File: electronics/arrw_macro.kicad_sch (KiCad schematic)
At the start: 15 parts, among them J13 Conn_01x04, J14 Conn_01x04, J15 Conn_01x04, J16 Conn_01x04, SW59 SW_SPST, SW60 SW_SPST, SW61 SW_SPST, SW62 SW_SPST, SW63 SW_SPST, SW64 SW_SPST, SW65 SW_SPST, SW66 SW_SPST, SW67 SW_SPST, SW68 SW_SPST, U4 MAX7314AEG+

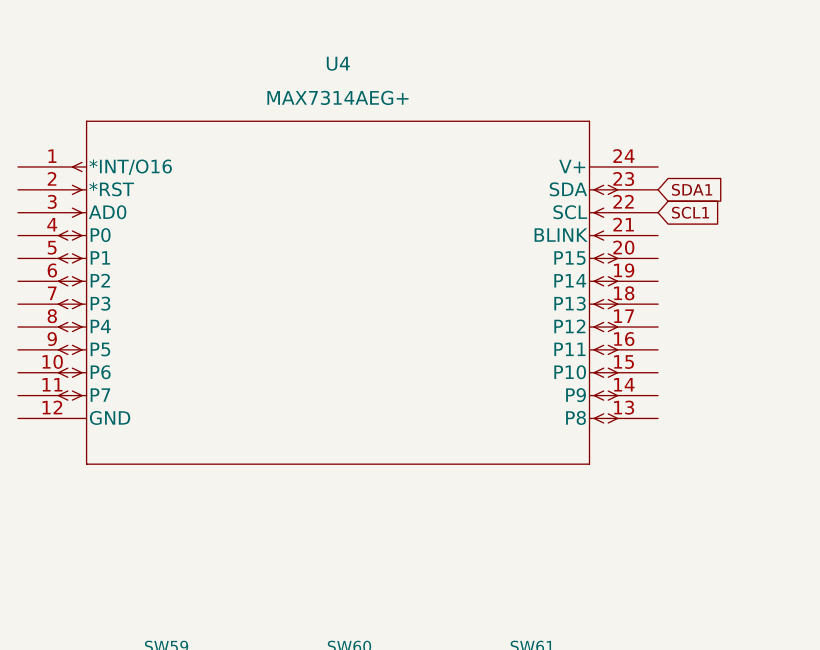
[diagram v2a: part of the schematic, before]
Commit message: change IO expander
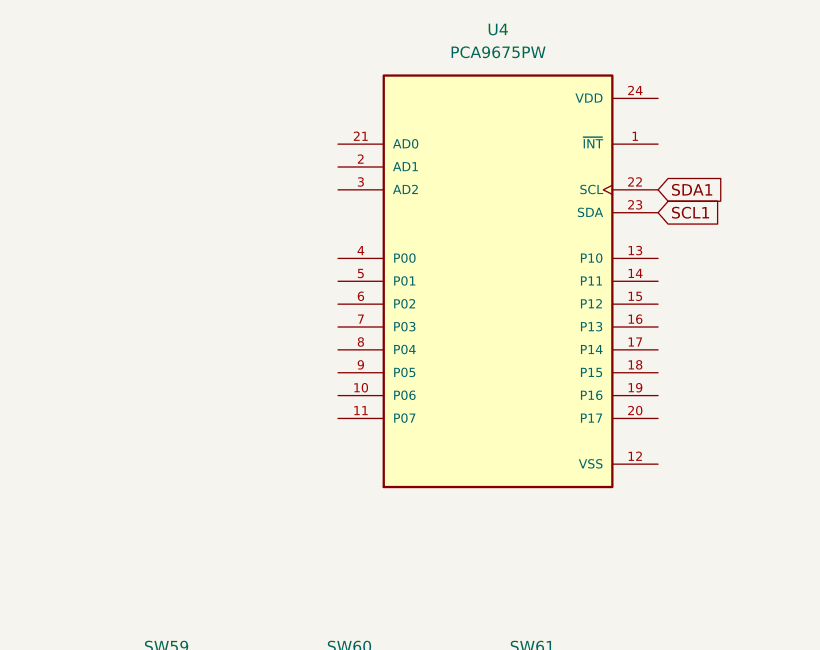
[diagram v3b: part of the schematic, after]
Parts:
- removed U4: MAX7314AEG+, MAX7314AEG:MAX7314AEG&plus_, symbol MAX7314AEG:MAX7314AEG+
- added U4: PCA9675PW, PCA9675PW:SOP65P640X110-24N, symbol PCA9675PW_118:PCA9675PW
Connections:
- net SCL1: now also U4.23 (SDA)
- net SDA1: now also U4.22 (SCL)
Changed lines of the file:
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@@
     (pin "1")
   )
-  (symbol (lib_id "MAX7314AEG:MAX7314AEG+") (at 52.07 46.99 0) (unit 1)
+  (symbol (lib_id "power:GND") (at 205.74 78.74 270) (unit 1)
     (in_bom yes) (on_board yes) (fields_autoplaced)
-    (property "Reference" "U4" (id 0) (at 87.63 35.56 0)
-      (effects (font (size 1.524 1.524)))
+    (property "Reference" "#PWR035" (id 0) (at 199.39 78.74 0)
+      (effects (font (size 1.27 1.27)) hide)
     )
-    (property "Value" "MAX7314AEG+" (id 1) (at 87.63 39.37 0)
-      (effects (font (size 1.524 1.524)))
+    (property "Value" "GND" (id 1) (at 201.93 78.7399 90)
+      (effects (font (size 1.27 1.27)) (justify right))
     )
-    (property "Footprint" "MAX7314AEG:MAX7314AEG&plus_" (id 2) (at 87.63 40.894 0)
-      (effects (font (size 1.524 1.524)) hide)
+    (property "Footprint" "" (id 2) (at 205.74 78.74 0)
+      (effects (font (size 1.27 1.27)) hide)
     )
-    (property "Datasheet" "${OSHMOUNT_LIBRARY}/MAX7314AEG/MAX7314AEG+.pdf" (id 3) (at 52.07 46.99 0)
-      (effects (font (size 1.524 1.524)) hide)
+    (property "Datasheet" "" (id 3) (at 205.74 78.74 0)
+      (effects (font (size 1.27 1.27)) hide)
+    )
+    (pin "1")
+  )
+  (symbol (lib_id "PCA9675PW_118:PCA9675PW") (at 105.41 59.69 0) (unit 1)
+    (in_bom yes) (on_board yes) (fields_autoplaced)
+    (property "Reference" "U4" (id 0) (at 105.41 31.75 0))
+    (property "Value" "PCA9675PW" (id 1) (at 105.41 34.29 0))
+    (property "Footprint" "PCA9675PW:SOP65P640X110-24N" (id 2) (at 105.41 59.69 0)
+      (effects (font (size 1.27 1.27)) (justify left bottom) hide)
+    )
+    (property "Datasheet" "${OSHMOUNT_LIBRARY}/PCA9675PW/datasheet.pdf" (id 3) (at 105.41 59.69 0)
+      (effects (font (size 1.27 1.27)) (justify left bottom) hide)
+    )
+    (property "E1_NOM" "4.4" (id 4) (at 105.41 59.69 0)
+      (effects (font (size 1.27 1.27)) (justify left bottom) hide)
+    )
+    (property "L1_MIN" "" (id 5) (at 105.41 59.69 0)
+      (effects (font (size 1.27 1.27)) (justify left bottom) hide)
+    )
+    (property "D1_NOM" "" (id 6) (at 105.41 59.69 0)
+      (effects (font (size 1.27 1.27)) (justify left bottom) hide)
+    )
+    (property "STANDARD" "IPC 7351B" (id 7) (at 105.41 59.69 0)
+      (effects (font (size 1.27 1.27)) (justify left bottom) hide)
+    )
+    (property "L1_MAX" "" (id 8) (at 105.41 59.69 0)
+      (effects (font (size 1.27 1.27)) (justify left bottom) hide)
+    )
+    (property "PACKAGE_TYPE" "" (id 9) (at 105.41 59.69 0)
+      (effects (font (size 1.27 1.27)) (justify left bottom) hide)
+    )
+    (property "PINS" "" (id 10) (at 105.41 59.69 0)
+      (effects (font (size 1.27 1.27)) (justify left bottom) hide)
+    )
+    (property "B_NOM" "0.245" (id 11) (at 105.41 59.69 0)
+      (effects (font (size 1.27 1.27)) (justify left bottom) hide)
+    )
+    (property "A1_MIN" "0.05" (id 12) (at 105.41 59.69 0)
+      (effects (font (size 1.27 1.27)) (justify left bottom) hide)
+    )
+    (property "D_MAX" "7.9" (id 13) (at 105.41 59.69 0)
+      (effects (font (size 1.27 1.27)) (justify left bottom) hide)
+    )
+    (property "D_MIN" "7.7" (id 14) (at 105.41 59.69 0)
+      (effects (font (size 1.27 1.27)) (justify left bottom) hide)
+    )
+    (property "E_MIN" "6.2" (id 15) (at 105.41 59.69 0)
+      (effects (font (size 1.27 1.27)) (justify left bottom) hide)
+    )
+    (property "VACANCIES" "" (id 16) (at 105.41 59.69 0)
+      (effects (font (size 1.27 1.27)) (justify left bottom) hide)
+    )
+    (property "E1_MIN" "4.3" (id 17) (at 105.41 59.69 0)
+      (effects (font (size 1.27 1.27)) (justify left bottom) hide)
+    )
+    (property "SNAPEDA_PACKAGE_ID" "" (id 18) (at 105.41 59.69 0)
+      (effects (font (size 1.27 1.27)) (justify left bottom) hide)
+    )
+    (property "MANUFACTURER" "NXP" (id 19) (at 105.41 59.69 0)
+      (effects (font (size 1.27 1.27)) (justify left bottom) hide)
+    )
+    (property "E1_MAX" "4.5" (id 20) (at 105.41 59.69 0)
+      (effects (font (size 1.27 1.27)) (justify left bottom) hide)
+    )
+    (property "DMIN" "" (id 21) (at 105.41 59.69 0)
+      (effects (font (size 1.27 1.27)) (justify left bottom) hide)
+    )
+    (property "B_MAX" "0.3" (id 22) (at 105.41 59.69 0)
+      (effects (font (size 1.27 1.27)) (justify left bottom) hide)
+    )
+    (property "A_NOM" "1.1" (id 23) (at 105.41 59.69 0)
+      (effects (font (size 1.27 1.27)) (justify left bottom) hide)
+    )
+    (property "D1_MAX" "" (id 24) (at 105.41 59.69 0)
+      (effects (font (size 1.27 1.27)) (justify left bottom) hide)
+    )
+    (property "DNOM" "" (id 25) (at 105.41 59.69 0)
+      (effects (font (size 1.27 1.27)) (justify left bottom) hide)
+    )
+    (property "PARTREV" "Rev. 2 — 3 October 2011" (id 26) (at 105.41 59.69 0)
+      (effects (font (size 1.27 1.27)) (justify left bottom) hide)
+    )
+    (property "D1_MIN" "" (id 27) (at 105.41 59.69 0)
+      (effects (font (size 1.27 1.27)) (justify left bottom) hide)
+    )
+    (property "DMAX" "" (id 28) (at 105.41 59.69 0)
+      (effects (font (size 1.27 1.27)) (justify left bottom) hide)
+    )
+    (property "A_MIN" "1.1" (id 29) (at 105.41 59.69 0)
+      (effects (font (size 1.27 1.27)) (justify left bottom) hide)
+    )
+    (property "B_MIN" "0.19" (id 30) (at 105.41 59.69 0)
+      (effects (font (size 1.27 1.27)) (justify left bottom) hide)
+    )
+    (property "PIN_COUNT" "24.0" (id 31) (at 105.41 59.69 0)
+      (effects (font (size 1.27 1.27)) (justify left bottom) hide)
+    )
+    (property "L1_NOM" "" (id 32) (at 105.41 59.69 0)
+      (effects (font (size 1.27 1.27)) (justify left bottom) hide)
+    )
+    (property "D_NOM" "7.8" (id 33) (at 105.41 59.69 0)
+      (effects (font (size 1.27 1.27)) (justify left bottom) hide)
+    )
+    (property "E_MAX" "6.6" (id 34) (at 105.41 59.69 0)
+      (effects (font (size 1.27 1.27)) (justify left bottom) hide)
+    )
+    (property "A_MAX" "1.1" (id 35) (at 105.41 59.69 0)
+      (effects (font (size 1.27 1.27)) (justify left bottom) hide)
+    )
+    (property "L_MIN" "0.5" (id 36) (at 105.41 59.69 0)
+      (effects (font (size 1.27 1.27)) (justify left bottom) hide)
+    )
+    (property "D2_MAX" "0.0" (id 37) (at 105.41 59.69 0)
+      (effects (font (size 1.27 1.27)) (justify left bottom) hide)
+    )
+    (property "EMAX" "" (id 38) (at 105.41 59.69 0)
+      (effects (font (size 1.27 1.27)) (justify left bottom) hide)
+    )
+    (property "E2_MAX" "0.0" (id 39) (at 105.41 59.69 0)
+      (effects (font (size 1.27 1.27)) (justify left bottom) hide)
+    )
+    (property "L_NOM" "0.625" (id 40) (at 105.41 59.69 0)
+      (effects (font (size 1.27 1.27)) (justify left bottom) hide)
+    )
+    (property "ENOM" "0.65" (id 41) (at 105.41 59.69 0)
+      (effects (font (size 1.27 1.27)) (justify left bottom) hide)
+    )
+    (property "EMIN" "" (id 42) (at 105.41 59.69 0)
+      (effects (font (size 1.27 1.27)) (justify left bottom) hide)
+    )
+    (property "E_NOM" "6.4" (id 43) (at 105.41 59.69 0)
+      (effects (font (size 1.27 1.27)) (justify left bottom) hide)
+    )
+    (property "L_MAX" "0.75" (id 44) (at 105.41 59.69 0)
+      (effects (font (size 1.27 1.27)) (justify left bottom) hide)
     )
     (pin "1")
@@
     (pin "9")
   )
-  (symbol (lib_id "power:GND") (at 205.74 78.74 270) (unit 1)
-    (in_bom yes) (on_board yes) (fields_autoplaced)
-    (property "Reference" "#PWR035" (id 0) (at 199.39 78.74 0)
-      (effects (font (size 1.27 1.27)) hide)
-    )
-    (property "Value" "GND" (id 1) (at 201.93 78.7399 90)
-      (effects (font (size 1.27 1.27)) (justify right))
-    )
-    (property "Footprint" "" (id 2) (at 205.74 78.74 0)
-      (effects (font (size 1.27 1.27)) hide)
-    )
-    (property "Datasheet" "" (id 3) (at 205.74 78.74 0)
-      (effects (font (size 1.27 1.27)) hide)
-    )
-    (pin "1")
-  )
   (symbol (lib_name "SW_SPST_22") (lib_id "Kailh:SW_SPST") (at 68.58 106.68 0) (unit 1)

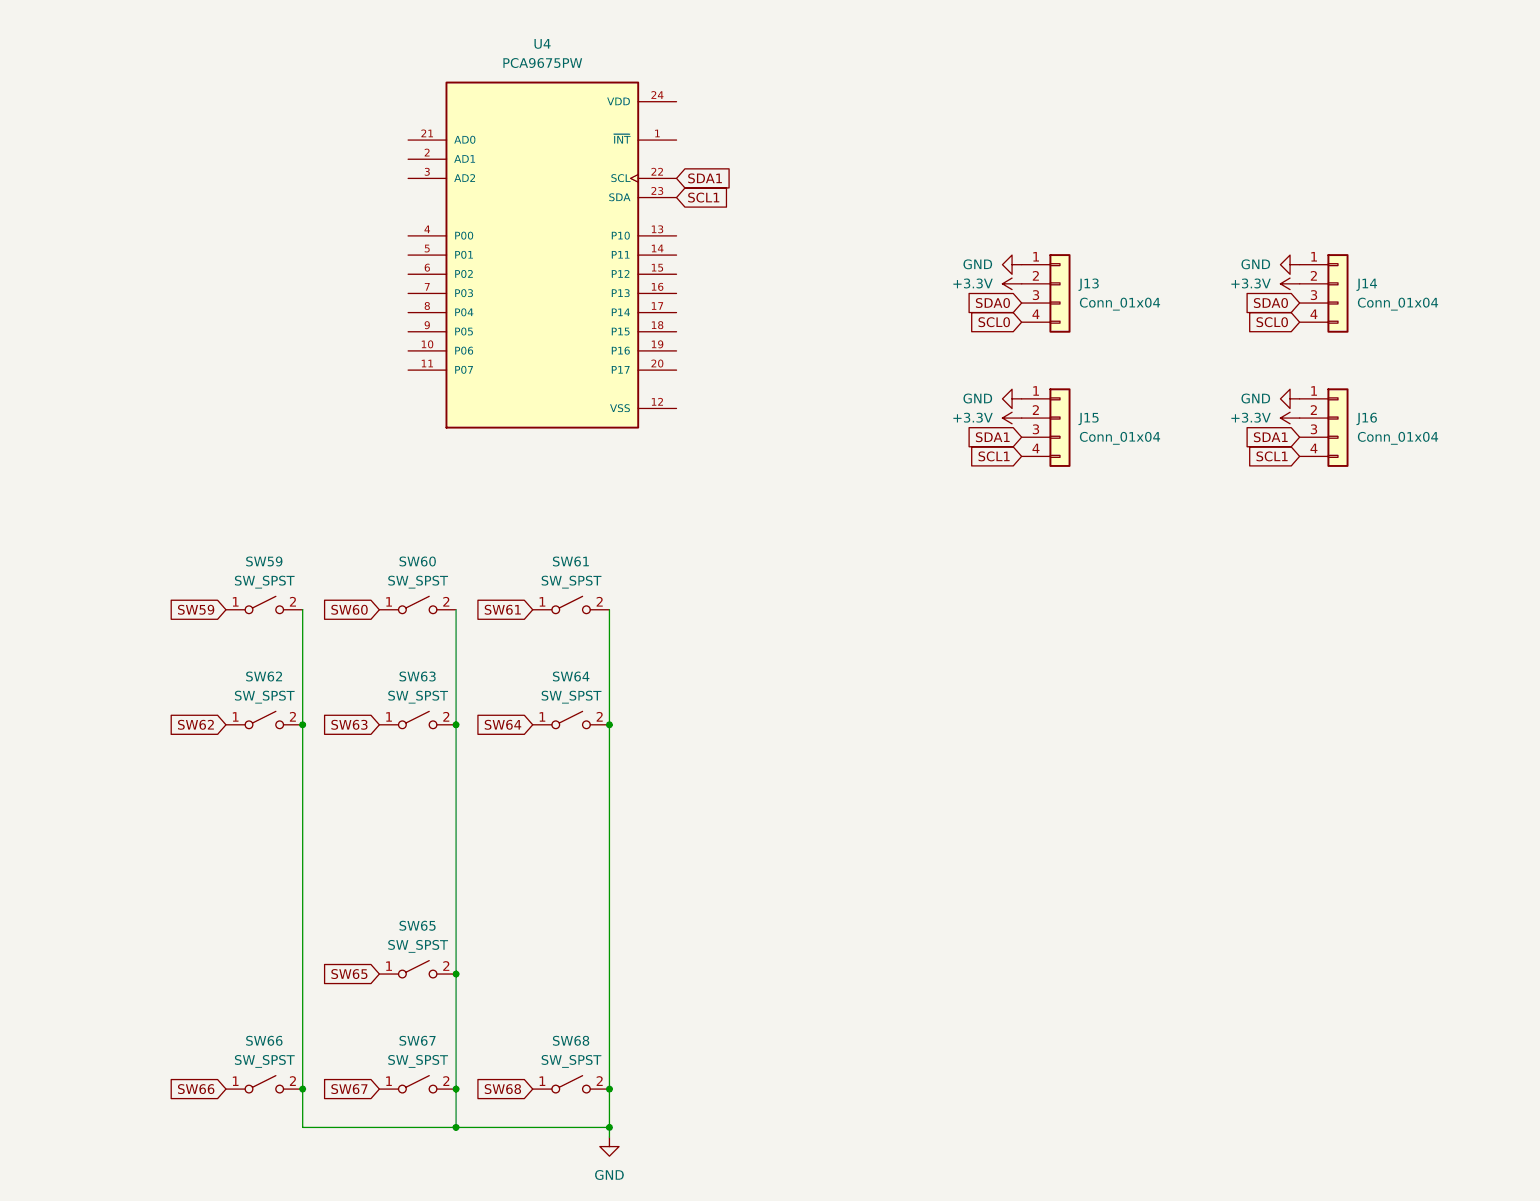
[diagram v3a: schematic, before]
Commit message: begin matrix via diodes
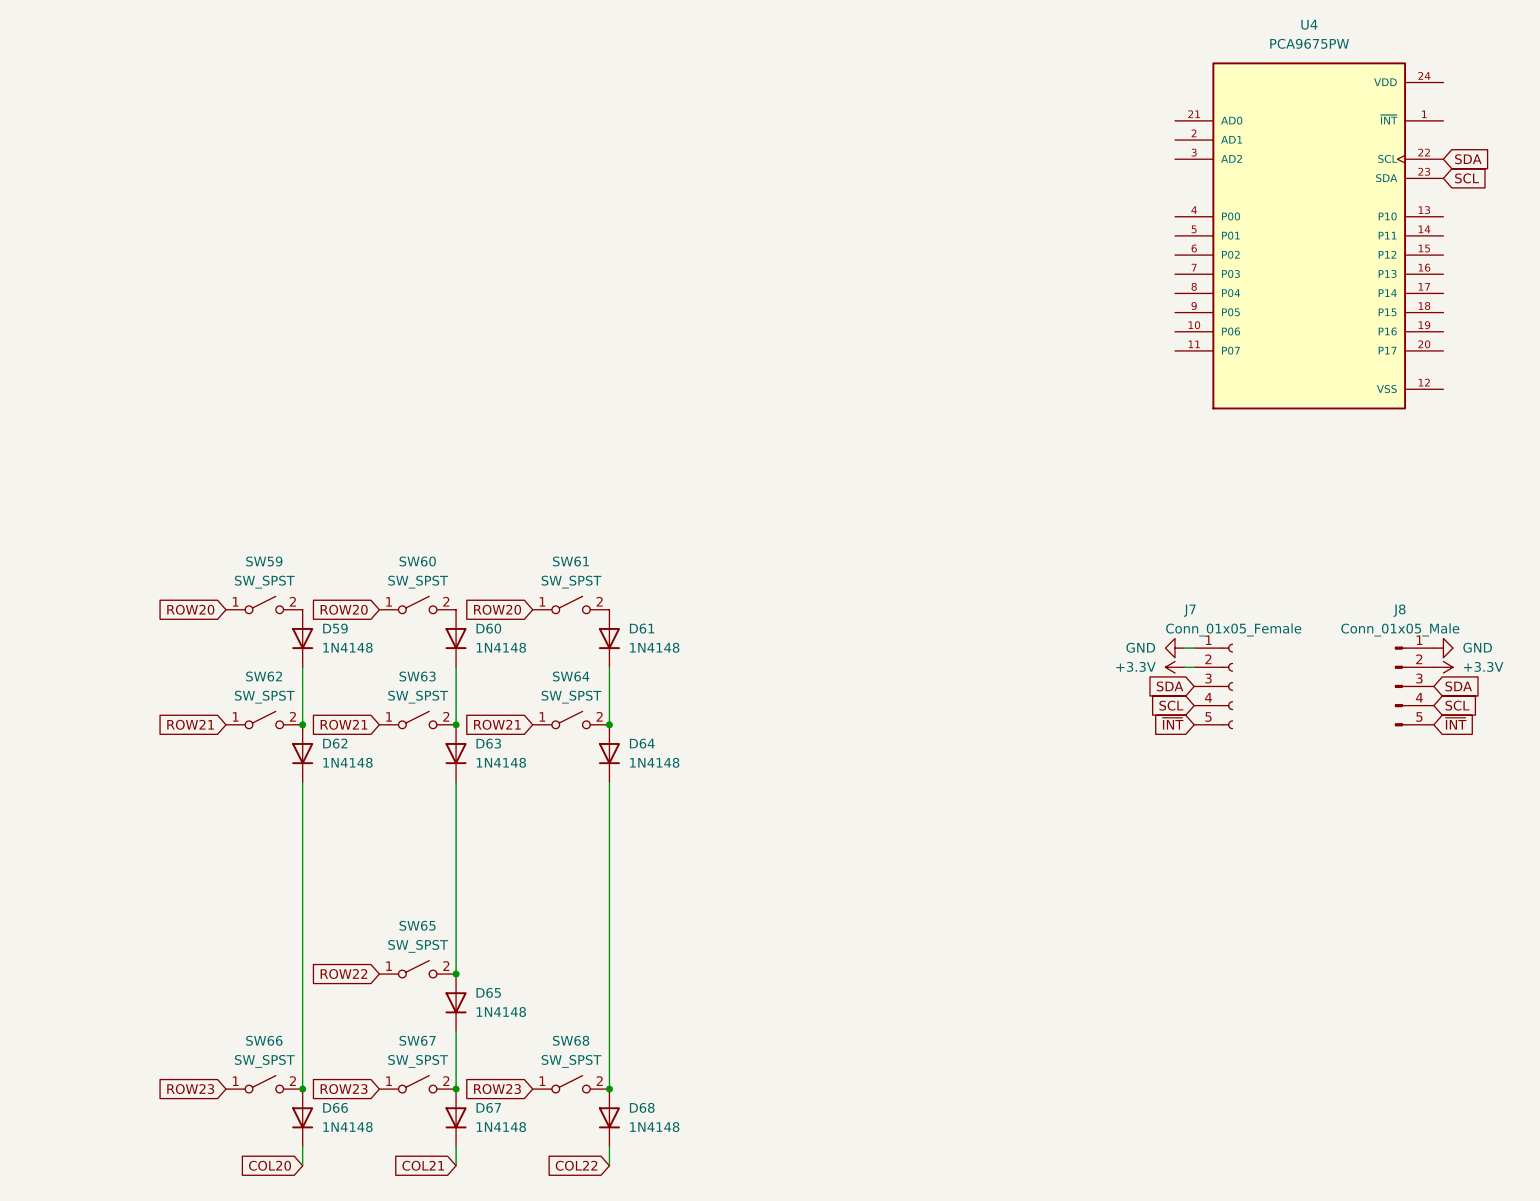
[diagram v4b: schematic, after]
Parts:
- removed J13, J14, J15, J16: Conn_01x04, symbol Connector_Generic:Conn_01x04
- added D59, D60, D61, D62, D63, D64, D65, D66, D67, D68: 1N4148, Diode_SMD:D_SOD-123, symbol Diode:1N4148W
- added J7: Conn_01x05_Female, Connector_PinHeader_2.54mm:PinHeader_1x05_P2.54mm_Vertical, symbol Connector:Conn_01x05_Female
- added J8: Conn_01x05_Male, Connector_PinHeader_2.54mm:PinHeader_1x05_P2.54mm_Vertical, symbol Connector:Conn_01x05_Male
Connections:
- net SW60 is gone; now on net ROW20: SW60.1 (A)
- net SW61 is gone; now on net ROW20: SW61.1 (A)
- net SW63 is gone; now on net ROW21: SW63.1 (A)
- net SW64 is gone; now on net ROW21: SW64.1 (A)
- net SW67 is gone; now on net ROW23: SW67.1 (A)
- net SW68 is gone; now on net ROW23: SW68.1 (A)
- net +3V3: now also J7.2 (Pin_2), J8.2 (Pin_2)
- net GND: now also J7.1 (Pin_1), J8.1 (Pin_1); no longer SW59.2 (B), SW60.2 (B), SW61.2 (B), SW62.2 (B), SW63.2 (B), SW64.2 (B), SW65.2 (B), SW66.2 (B), SW67.2 (B), SW68.2 (B)
- net SCL1 renamed SCL
- net SCL: now also J7.4 (Pin_4), J8.4 (Pin_4)
- net SDA1 renamed SDA
- net SDA: now also J7.3 (Pin_3), J8.3 (Pin_3)
- net SW59 renamed ROW20
- net SW62 renamed ROW21
- net SW65 renamed ROW22
- net SW66 renamed ROW23
- new net: D63.1 (K), D65.2 (A), SW65.2 (B)
- new net: D65.1 (K), D67.2 (A), SW67.2 (B)
- new net: D60.1 (K), D63.2 (A), SW63.2 (B)
- new net: D60.2 (A), SW60.2 (B)
- new net: D64.1 (K), D68.2 (A), SW68.2 (B)
- new net: D61.1 (K), D64.2 (A), SW64.2 (B)
- new net: D61.2 (A), SW61.2 (B)
- new net: D59.2 (A), SW59.2 (B)
- new net: D59.1 (K), D62.2 (A), SW62.2 (B)
- new net: D62.1 (K), D66.2 (A), SW66.2 (B)
- new net COL20: D66.1 (K)
- new net COL21: D67.1 (K)
- new net COL22: D68.1 (K)
- new net ~{INT}: J7.5 (Pin_5), J8.5 (Pin_5)
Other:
- moved on the sheet: U4
